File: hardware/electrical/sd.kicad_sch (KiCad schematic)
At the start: 9 parts, among them J3 Micro_SD_Card_Det2

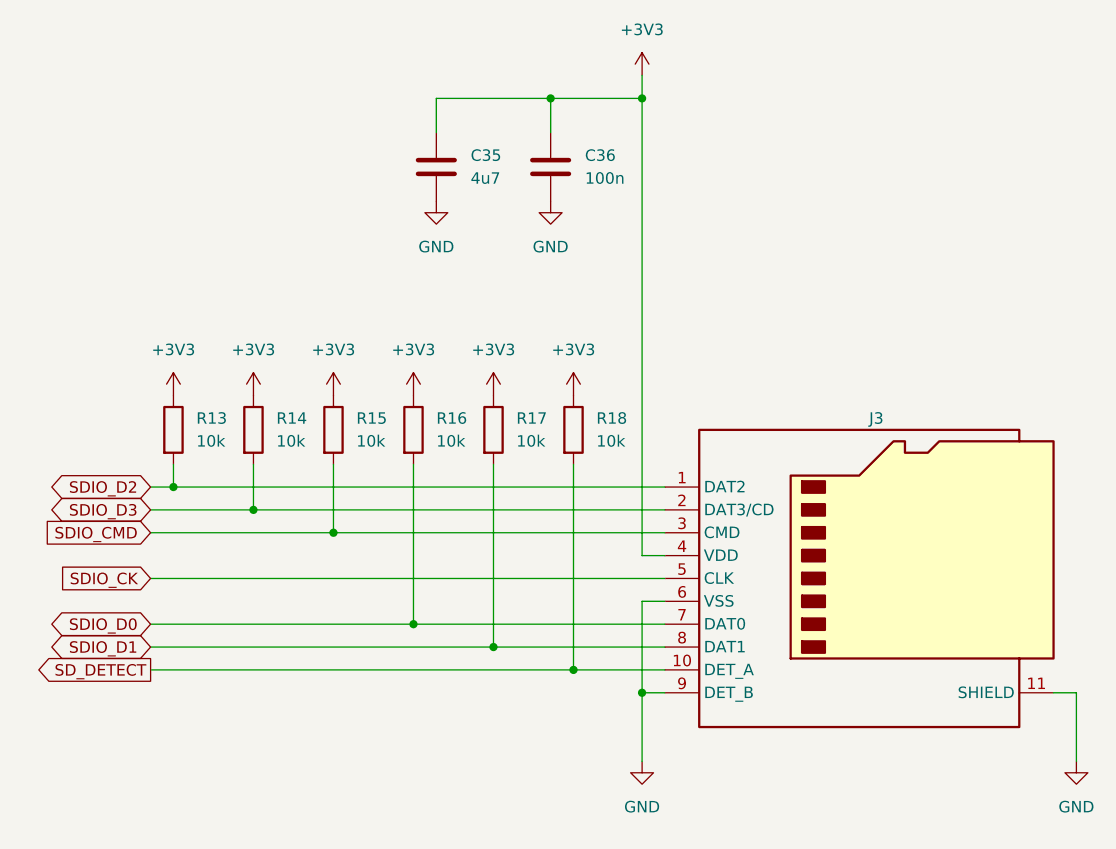
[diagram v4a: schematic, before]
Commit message: Use VDD in place of +3.3V more extensively
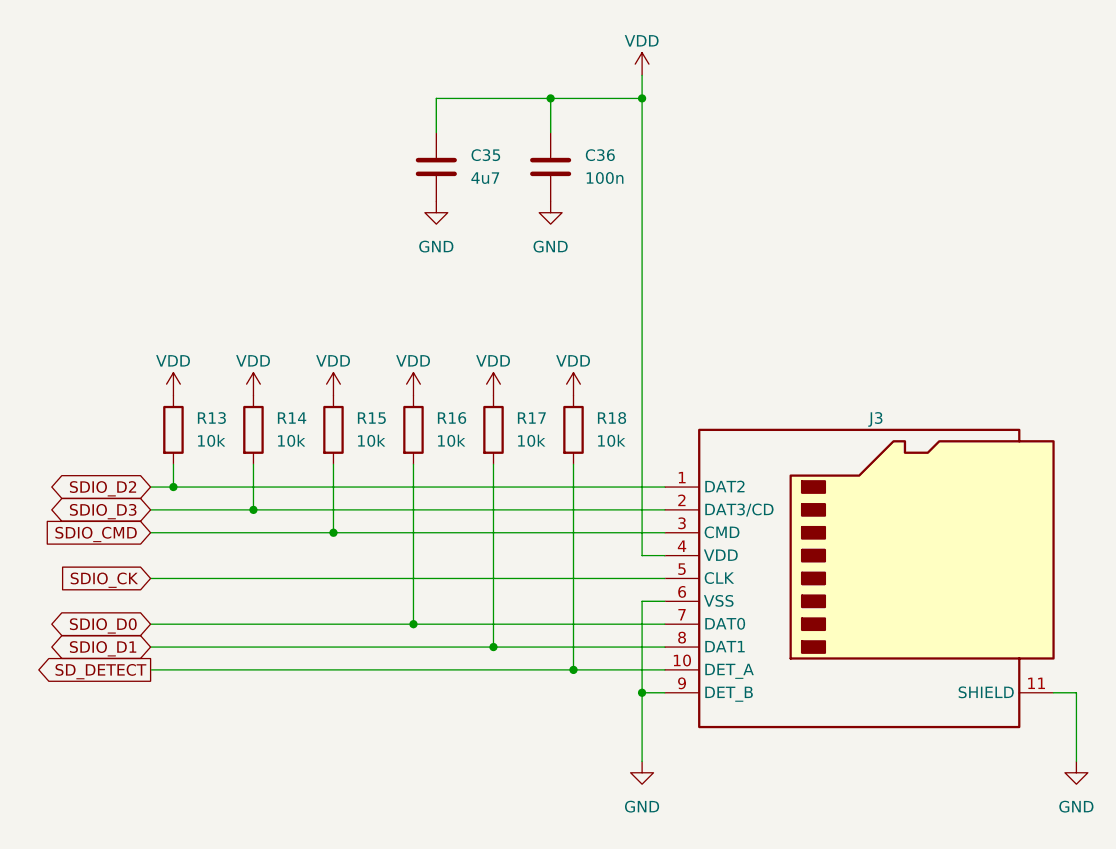
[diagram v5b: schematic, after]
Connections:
- net +3V3 renamed VDD
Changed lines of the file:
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@@
     )
   )
-  (symbol (lib_id "power:+3V3") (at 140.97 88.9 0) (unit 1)
-    (in_bom yes) (on_board yes) (dnp no)
-    (property "Reference" "#PWR060" (at 140.97 92.71 0)
-      (effects (font (size 1.27 1.27)) hide)
-    )
-    (property "Value" "+3V3" (at 140.97 83.82 0)
-      (effects (font (size 1.27 1.27)))
-    )
-    (property "Footprint" "" (at 140.97 88.9 0)
-      (effects (font (size 1.27 1.27)) hide)
-    )
-    (property "Datasheet" "" (at 140.97 88.9 0)
-      (effects (font (size 1.27 1.27)) hide)
-    )
-    (pin "1")
-    (instances
-      (project "3885"
-        (path "/7363a4f0-2da1-4086-abed-ea6709c3a185/6cde842e-a6be-40ad-bea6-4575bf07edd2"
-          (reference "#PWR060") (unit 1)
+  (symbol (lib_id "power:VDD") (at 114.3 88.9 0) (unit 1)
+    (in_bom yes) (on_board yes) (dnp no) (fields_autoplaced)
+    (property "Reference" "#PWR056" (at 114.3 92.71 0)
+      (effects (font (size 1.27 1.27)) hide)
+    )
+    (property "Value" "VDD" (at 114.3 85.09 0)
+      (effects (font (size 1.27 1.27)))
+    )
+    (property "Footprint" "" (at 114.3 88.9 0)
+      (effects (font (size 1.27 1.27)) hide)
+    )
+    (property "Datasheet" "" (at 114.3 88.9 0)
+      (effects (font (size 1.27 1.27)) hide)
+    )
+    (pin "1")
+    (instances
+      (project "3885"
+        (path "/7363a4f0-2da1-4086-abed-ea6709c3a185/6cde842e-a6be-40ad-bea6-4575bf07edd2"
+          (reference "#PWR056") (unit 1)
         )
       )
@@
     )
   )
+  (symbol (lib_id "power:VDD") (at 149.86 88.9 0) (unit 1)
+    (in_bom yes) (on_board yes) (dnp no) (fields_autoplaced)
+    (property "Reference" "#PWR062" (at 149.86 92.71 0)
+      (effects (font (size 1.27 1.27)) hide)
+    )
+    (property "Value" "VDD" (at 149.86 85.09 0)
+      (effects (font (size 1.27 1.27)))
+    )
+    (property "Footprint" "" (at 149.86 88.9 0)
+      (effects (font (size 1.27 1.27)) hide)
+    )
+    (property "Datasheet" "" (at 149.86 88.9 0)
+      (effects (font (size 1.27 1.27)) hide)
+    )
+    (pin "1")
+    (instances
+      (project "3885"
+        (path "/7363a4f0-2da1-4086-abed-ea6709c3a185/6cde842e-a6be-40ad-bea6-4575bf07edd2"
+          (reference "#PWR062") (unit 1)
+        )
+      )
+    )
+  )
   (symbol (lib_id "Device:R") (at 105.41 92.71 0) (unit 1)
     (in_bom yes) (on_board yes) (dnp no) (fields_autoplaced)
@@
     )
   )
+  (symbol (lib_id "power:VDD") (at 105.41 88.9 0) (unit 1)
+    (in_bom yes) (on_board yes) (dnp no) (fields_autoplaced)
+    (property "Reference" "#PWR055" (at 105.41 92.71 0)
+      (effects (font (size 1.27 1.27)) hide)
+    )
+    (property "Value" "VDD" (at 105.41 85.09 0)
+      (effects (font (size 1.27 1.27)))
+    )
+    (property "Footprint" "" (at 105.41 88.9 0)
+      (effects (font (size 1.27 1.27)) hide)
+    )
+    (property "Datasheet" "" (at 105.41 88.9 0)
+      (effects (font (size 1.27 1.27)) hide)
+    )
+    (pin "1")
+    (instances
+      (project "3885"
+        (path "/7363a4f0-2da1-4086-abed-ea6709c3a185/6cde842e-a6be-40ad-bea6-4575bf07edd2"
+          (reference "#PWR055") (unit 1)
+        )
+      )
+    )
+  )
   (symbol (lib_id "Device:R") (at 123.19 92.71 0) (unit 1)
     (in_bom yes) (on_board yes) (dnp no) (fields_autoplaced)
@@
     )
   )
+  (symbol (lib_id "power:VDD") (at 157.48 53.34 0) (unit 1)
+    (in_bom yes) (on_board yes) (dnp no) (fields_autoplaced)
+    (property "Reference" "#PWR063" (at 157.48 57.15 0)
+      (effects (font (size 1.27 1.27)) hide)
+    )
+    (property "Value" "VDD" (at 157.48 49.53 0)
+      (effects (font (size 1.27 1.27)))
+    )
+    (property "Footprint" "" (at 157.48 53.34 0)
+      (effects (font (size 1.27 1.27)) hide)
+    )
+    (property "Datasheet" "" (at 157.48 53.34 0)
+      (effects (font (size 1.27 1.27)) hide)
+    )
+    (pin "1")
+    (instances
+      (project "3885"
+        (path "/7363a4f0-2da1-4086-abed-ea6709c3a185/6cde842e-a6be-40ad-bea6-4575bf07edd2"
+          (reference "#PWR063") (unit 1)
+        )
+      )
+    )
+  )
   (symbol (lib_id "Device:R") (at 132.08 92.71 0) (unit 1)
     (in_bom yes) (on_board yes) (dnp no) (fields_autoplaced)
@@
     )
   )
-  (symbol (lib_id "power:+3V3") (at 132.08 88.9 0) (unit 1)
-    (in_bom yes) (on_board yes) (dnp no)
+  (symbol (lib_id "power:VDD") (at 132.08 88.9 0) (unit 1)
+    (in_bom yes) (on_board yes) (dnp no) (fields_autoplaced)
     (property "Reference" "#PWR058" (at 132.08 92.71 0)
       (effects (font (size 1.27 1.27)) hide)
     )
-    (property "Value" "+3V3" (at 132.08 83.82 0)
+    (property "Value" "VDD" (at 132.08 85.09 0)
       (effects (font (size 1.27 1.27)))
     )
@@
     )
   )
-  (symbol (lib_id "power:+3V3") (at 157.48 53.34 0) (unit 1)
-    (in_bom yes) (on_board yes) (dnp no) (fields_autoplaced)
-    (property "Reference" "#PWR063" (at 157.48 57.15 0)
-      (effects (font (size 1.27 1.27)) hide)
-    )
-    (property "Value" "+3V3" (at 157.48 48.26 0)
-      (effects (font (size 1.27 1.27)))
-    )
-    (property "Footprint" "" (at 157.48 53.34 0)
-      (effects (font (size 1.27 1.27)) hide)
-    )
-    (property "Datasheet" "" (at 157.48 53.34 0)
-      (effects (font (size 1.27 1.27)) hide)
-    )
-    (pin "1")
-    (instances
-      (project "3885"
-        (path "/7363a4f0-2da1-4086-abed-ea6709c3a185/6cde842e-a6be-40ad-bea6-4575bf07edd2"
-          (reference "#PWR063") (unit 1)
-        )
-      )
-    )
-  )
   (symbol (lib_id "Device:C") (at 134.62 63.5 0) (unit 1)
     (in_bom yes) (on_board yes) (dnp no) (fields_autoplaced)
@@
     )
   )
-  (symbol (lib_id "power:+3V3") (at 105.41 88.9 0) (unit 1)
-    (in_bom yes) (on_board yes) (dnp no) (fields_autoplaced)
-    (property "Reference" "#PWR055" (at 105.41 92.71 0)
-      (effects (font (size 1.27 1.27)) hide)
-    )
-    (property "Value" "+3V3" (at 105.41 83.82 0)
-      (effects (font (size 1.27 1.27)))
-    )
-    (property "Footprint" "" (at 105.41 88.9 0)
-      (effects (font (size 1.27 1.27)) hide)
-    )
-    (property "Datasheet" "" (at 105.41 88.9 0)
-      (effects (font (size 1.27 1.27)) hide)
-    )
-    (pin "1")
-    (instances
-      (project "3885"
-        (path "/7363a4f0-2da1-4086-abed-ea6709c3a185/6cde842e-a6be-40ad-bea6-4575bf07edd2"
-          (reference "#PWR055") (unit 1)
+  (symbol (lib_id "power:VDD") (at 140.97 88.9 0) (unit 1)
+    (in_bom yes) (on_board yes) (dnp no) (fields_autoplaced)
+    (property "Reference" "#PWR060" (at 140.97 92.71 0)
+      (effects (font (size 1.27 1.27)) hide)
+    )
+    (property "Value" "VDD" (at 140.97 85.09 0)
+      (effects (font (size 1.27 1.27)))
+    )
+    (property "Footprint" "" (at 140.97 88.9 0)
+      (effects (font (size 1.27 1.27)) hide)
+    )
+    (property "Datasheet" "" (at 140.97 88.9 0)
+      (effects (font (size 1.27 1.27)) hide)
+    )
+    (pin "1")
+    (instances
+      (project "3885"
+        (path "/7363a4f0-2da1-4086-abed-ea6709c3a185/6cde842e-a6be-40ad-bea6-4575bf07edd2"
+          (reference "#PWR060") (unit 1)
         )
       )
@@
     )
   )
-  (symbol (lib_id "power:+3V3") (at 114.3 88.9 0) (unit 1)
-    (in_bom yes) (on_board yes) (dnp no) (fields_autoplaced)
-    (property "Reference" "#PWR056" (at 114.3 92.71 0)
-      (effects (font (size 1.27 1.27)) hide)
-    )
-    (property "Value" "+3V3" (at 114.3 83.82 0)
-      (effects (font (size 1.27 1.27)))
-    )
-    (property "Footprint" "" (at 114.3 88.9 0)
-      (effects (font (size 1.27 1.27)) hide)
-    )
-    (property "Datasheet" "" (at 114.3 88.9 0)
-      (effects (font (size 1.27 1.27)) hide)
-    )
-    (pin "1")
-    (instances
-      (project "3885"
-        (path "/7363a4f0-2da1-4086-abed-ea6709c3a185/6cde842e-a6be-40ad-bea6-4575bf07edd2"
-          (reference "#PWR056") (unit 1)
+  (symbol (lib_id "power:VDD") (at 123.19 88.9 0) (unit 1)
+    (in_bom yes) (on_board yes) (dnp no) (fields_autoplaced)
+    (property "Reference" "#PWR057" (at 123.19 92.71 0)
+      (effects (font (size 1.27 1.27)) hide)
+    )
+    (property "Value" "VDD" (at 123.19 85.09 0)
+      (effects (font (size 1.27 1.27)))
+    )
+    (property "Footprint" "" (at 123.19 88.9 0)
+      (effects (font (size 1.27 1.27)) hide)
+    )
+    (property "Datasheet" "" (at 123.19 88.9 0)
+      (effects (font (size 1.27 1.27)) hide)
+    )
+    (pin "1")
+    (instances
+      (project "3885"
+        (path "/7363a4f0-2da1-4086-abed-ea6709c3a185/6cde842e-a6be-40ad-bea6-4575bf07edd2"
+          (reference "#PWR057") (unit 1)
         )
       )
@@
         )
       )
-    )
-  )
-  (symbol (lib_id "power:+3V3") (at 149.86 88.9 0) (unit 1)
-    (in_bom yes) (on_board yes) (dnp no)
-    (property "Reference" "#PWR062" (at 149.86 92.71 0)
-      (effects (font (size 1.27 1.27)) hide)
-    )
-    (property "Value" "+3V3" (at 149.86 83.82 0)
-      (effects (font (size 1.27 1.27)))
-    )
-    (property "Footprint" "" (at 149.86 88.9 0)
-      (effects (font (size 1.27 1.27)) hide)
-    )
-    (property "Datasheet" "" (at 149.86 88.9 0)
-      (effects (font (size 1.27 1.27)) hide)
-    )
-    (pin "1")
-    (instances
-      (project "3885"
-        (path "/7363a4f0-2da1-4086-abed-ea6709c3a185/6cde842e-a6be-40ad-bea6-4575bf07edd2"
-          (reference "#PWR062") (unit 1)
-        )
-      )
-    )
-  )
-  (symbol (lib_id "power:+3V3") (at 123.19 88.9 0) (unit 1)
-    (in_bom yes) (on_board yes) (dnp no) (fields_autoplaced)
-    (property "Reference" "#PWR057" (at 123.19 92.71 0)
-      (effects (font (size 1.27 1.27)) hide)
-    )
-    (property "Value" "+3V3" (at 123.19 83.82 0)
-      (effects (font (size 1.27 1.27)))
-    )
-    (property "Footprint" "" (at 123.19 88.9 0)
-      (effects (font (size 1.27 1.27)) hide)
-    )
-    (property "Datasheet" "" (at 123.19 88.9 0)
-      (effects (font (size 1.27 1.27)) hide)
-    )
-    (pin "1")
-    (instances
-      (project "3885"
-        (path "/7363a4f0-2da1-4086-abed-ea6709c3a185/6cde842e-a6be-40ad-bea6-4575bf07edd2"
-          (reference "#PWR057") (unit 1)
-        )
-      )

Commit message: Component selection
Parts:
- C35: footprint (none) -> Capacitor_SMD:C_0402_1005Metric; LCSC Part # (none) -> C23733; Mfr (none) -> Samsung Electro-Mechanics; Mfr. Part # (none) -> CL05A475MP5NRNC
- C36: footprint (none) -> Capacitor_SMD:C_0402_1005Metric; LCSC Part # (none) -> C1525; Mfr (none) -> Samsung Electro-Mechanics; Mfr. Part # (none) -> CL05B104KO5NNNC
- J3: LCSC Part # (none) -> C381084; Mfr (none) -> XKB Connectivity; Mfr. Part # (none) -> XKTF-N02-N
- R13, R14, R15, R16, R17, R18: footprint (none) -> Resistor_SMD:R_0402_1005Metric; LCSC Part # (none) -> C25744; Mfr (none) -> UNI-ROYAL(Uniroyal Elec); Mfr. Part # (none) -> 0402WGF1002TCE
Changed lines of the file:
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@@
       (effects (font (size 1.27 1.27)) (justify left))
     )
-    (property "Footprint" "" (at 103.632 92.71 90)
-      (effects (font (size 1.27 1.27)) hide)
-    )
-    (property "Datasheet" "~" (at 105.41 92.71 0)
+    (property "Footprint" "Resistor_SMD:R_0402_1005Metric" (at 103.632 92.71 90)
+      (effects (font (size 1.27 1.27)) hide)
+    )
+    (property "Datasheet" "https://datasheet.lcsc.com/lcsc/2206010100_UNI-ROYAL-Uniroyal-Elec-0402WGF1002TCE_C25744.pdf" (at 105.41 92.71 0)
+      (effects (font (size 1.27 1.27)) hide)
+    )
+    (property "LCSC Part #" "C25744" (at 105.41 92.71 0)
+      (effects (font (size 1.27 1.27)) hide)
+    )
+    (property "Mfr" "UNI-ROYAL(Uniroyal Elec)" (at 105.41 92.71 0)
+      (effects (font (size 1.27 1.27)) hide)
+    )
+    (property "Mfr. Part #" "0402WGF1002TCE" (at 105.41 92.71 0)
       (effects (font (size 1.27 1.27)) hide)
     )
@@
       (effects (font (size 1.27 1.27)) (justify left))
     )
-    (property "Footprint" "" (at 121.412 92.71 90)
-      (effects (font (size 1.27 1.27)) hide)
-    )
-    (property "Datasheet" "~" (at 123.19 92.71 0)
+    (property "Footprint" "Resistor_SMD:R_0402_1005Metric" (at 121.412 92.71 90)
+      (effects (font (size 1.27 1.27)) hide)
+    )
+    (property "Datasheet" "https://datasheet.lcsc.com/lcsc/2206010100_UNI-ROYAL-Uniroyal-Elec-0402WGF1002TCE_C25744.pdf" (at 123.19 92.71 0)
+      (effects (font (size 1.27 1.27)) hide)
+    )
+    (property "LCSC Part #" "C25744" (at 123.19 92.71 0)
+      (effects (font (size 1.27 1.27)) hide)
+    )
+    (property "Mfr" "UNI-ROYAL(Uniroyal Elec)" (at 123.19 92.71 0)
+      (effects (font (size 1.27 1.27)) hide)
+    )
+    (property "Mfr. Part #" "0402WGF1002TCE" (at 123.19 92.71 0)
       (effects (font (size 1.27 1.27)) hide)
     )
@@
       (effects (font (size 1.27 1.27)) (justify left))
     )
-    (property "Footprint" "" (at 130.302 92.71 90)
-      (effects (font (size 1.27 1.27)) hide)
-    )
-    (property "Datasheet" "~" (at 132.08 92.71 0)
+    (property "Footprint" "Resistor_SMD:R_0402_1005Metric" (at 130.302 92.71 90)
+      (effects (font (size 1.27 1.27)) hide)
+    )
+    (property "Datasheet" "https://datasheet.lcsc.com/lcsc/2206010100_UNI-ROYAL-Uniroyal-Elec-0402WGF1002TCE_C25744.pdf" (at 132.08 92.71 0)
+      (effects (font (size 1.27 1.27)) hide)
+    )
+    (property "LCSC Part #" "C25744" (at 132.08 92.71 0)
+      (effects (font (size 1.27 1.27)) hide)
+    )
+    (property "Mfr" "UNI-ROYAL(Uniroyal Elec)" (at 132.08 92.71 0)
+      (effects (font (size 1.27 1.27)) hide)
+    )
+    (property "Mfr. Part #" "0402WGF1002TCE" (at 132.08 92.71 0)
       (effects (font (size 1.27 1.27)) hide)
     )
@@
       (effects (font (size 1.27 1.27)) hide)
     )
-    (property "Datasheet" "https://www.hirose.com/en/product/document?clcode=&productname=&series=DM3&documenttype=Catalog&lang=en&documentid=D49662_en" (at 185.42 106.68 0)
+    (property "Datasheet" "https://datasheet.lcsc.com/lcsc/2110151630_XKB-Connectivity-XKTF-N02-N_C381084.pdf" (at 185.42 106.68 0)
+      (effects (font (size 1.27 1.27)) hide)
+    )
+    (property "LCSC Part #" "C381084" (at 182.88 109.22 0)
+      (effects (font (size 1.27 1.27)) hide)
+    )
+    (property "Mfr" "XKB Connectivity" (at 182.88 109.22 0)
+      (effects (font (size 1.27 1.27)) hide)
+    )
+    (property "Mfr. Part #" "XKTF-N02-N" (at 182.88 109.22 0)
       (effects (font (size 1.27 1.27)) hide)
     )
@@
       (effects (font (size 1.27 1.27)) (justify left))
     )
-    (property "Footprint" "" (at 135.5852 67.31 0)
-      (effects (font (size 1.27 1.27)) hide)
-    )
-    (property "Datasheet" "~" (at 134.62 63.5 0)
+    (property "Footprint" "Capacitor_SMD:C_0402_1005Metric" (at 135.5852 67.31 0)
+      (effects (font (size 1.27 1.27)) hide)
+    )
+    (property "Datasheet" "https://datasheet.lcsc.com/lcsc/1810191211_Samsung-Electro-Mechanics-CL05A475MP5NRNC_C23733.pdf" (at 134.62 63.5 0)
+      (effects (font (size 1.27 1.27)) hide)
+    )
+    (property "LCSC Part #" "C23733" (at 134.62 63.5 0)
+      (effects (font (size 1.27 1.27)) hide)
+    )
+    (property "Mfr" "Samsung Electro-Mechanics" (at 134.62 63.5 0)
+      (effects (font (size 1.27 1.27)) hide)
+    )
+    (property "Mfr. Part #" "CL05A475MP5NRNC" (at 134.62 63.5 0)
       (effects (font (size 1.27 1.27)) hide)
     )
@@
       (effects (font (size 1.27 1.27)) (justify left))
     )
-    (property "Footprint" "" (at 148.2852 67.31 0)
-      (effects (font (size 1.27 1.27)) hide)
-    )
-    (property "Datasheet" "~" (at 147.32 63.5 0)
+    (property "Footprint" "Capacitor_SMD:C_0402_1005Metric" (at 148.2852 67.31 0)
+      (effects (font (size 1.27 1.27)) hide)
+    )
+    (property "Datasheet" "https://datasheet.lcsc.com/lcsc/1810191219_Samsung-Electro-Mechanics-CL05B104KO5NNNC_C1525.pdf" (at 147.32 63.5 0)
+      (effects (font (size 1.27 1.27)) hide)
+    )
+    (property "LCSC Part #" "C1525" (at 147.32 63.5 0)
+      (effects (font (size 1.27 1.27)) hide)
+    )
+    (property "Mfr" "Samsung Electro-Mechanics" (at 147.32 63.5 0)
+      (effects (font (size 1.27 1.27)) hide)
+    )
+    (property "Mfr. Part #" "CL05B104KO5NNNC" (at 147.32 63.5 0)
       (effects (font (size 1.27 1.27)) hide)
     )
@@
       (effects (font (size 1.27 1.27)) (justify left))
     )
-    (property "Footprint" "" (at 112.522 92.71 90)
-      (effects (font (size 1.27 1.27)) hide)
-    )
-    (property "Datasheet" "~" (at 114.3 92.71 0)
+    (property "Footprint" "Resistor_SMD:R_0402_1005Metric" (at 112.522 92.71 90)
+      (effects (font (size 1.27 1.27)) hide)
+    )
+    (property "Datasheet" "https://datasheet.lcsc.com/lcsc/2206010100_UNI-ROYAL-Uniroyal-Elec-0402WGF1002TCE_C25744.pdf" (at 114.3 92.71 0)
+      (effects (font (size 1.27 1.27)) hide)
+    )
+    (property "LCSC Part #" "C25744" (at 114.3 92.71 0)
+      (effects (font (size 1.27 1.27)) hide)
+    )
+    (property "Mfr" "UNI-ROYAL(Uniroyal Elec)" (at 114.3 92.71 0)
+      (effects (font (size 1.27 1.27)) hide)
+    )
+    (property "Mfr. Part #" "0402WGF1002TCE" (at 114.3 92.71 0)
       (effects (font (size 1.27 1.27)) hide)
     )
@@
       (effects (font (size 1.27 1.27)) (justify left))
     )
-    (property "Footprint" "" (at 148.082 92.71 90)
-      (effects (font (size 1.27 1.27)) hide)
-    )
-    (property "Datasheet" "~" (at 149.86 92.71 0)
+    (property "Footprint" "Resistor_SMD:R_0402_1005Metric" (at 148.082 92.71 90)
+      (effects (font (size 1.27 1.27)) hide)
+    )
+    (property "Datasheet" "https://datasheet.lcsc.com/lcsc/2206010100_UNI-ROYAL-Uniroyal-Elec-0402WGF1002TCE_C25744.pdf" (at 149.86 92.71 0)
+      (effects (font (size 1.27 1.27)) hide)
+    )
+    (property "LCSC Part #" "C25744" (at 149.86 92.71 0)
+      (effects (font (size 1.27 1.27)) hide)
+    )
+    (property "Mfr" "UNI-ROYAL(Uniroyal Elec)" (at 149.86 92.71 0)
+      (effects (font (size 1.27 1.27)) hide)
+    )
+    (property "Mfr. Part #" "0402WGF1002TCE" (at 149.86 92.71 0)
       (effects (font (size 1.27 1.27)) hide)
     )
@@
       (effects (font (size 1.27 1.27)) (justify left))
     )
-    (property "Footprint" "" (at 139.192 92.71 90)
-      (effects (font (size 1.27 1.27)) hide)
-    )
-    (property "Datasheet" "~" (at 140.97 92.71 0)
-      (effects (font (size 1.27 1.27)) hide)
-    )
+    (property "Footprint" "Resistor_SMD:R_0402_1005Metric" (at 139.192 92.71 90)
+      (effects (font (size 1.27 1.27)) hide)
+    )
+    (property "Datasheet" "https://datasheet.lcsc.com/lcsc/2206010100_UNI-ROYAL-Uniroyal-Elec-0402WGF1002TCE_C25744.pdf" (at 140.97 92.71 0)
+      (effects (font (size 1.27 1.27)) hide)
+    )
+    (property "LCSC Part #" "C25744" (at 140.97 92.71 0)
+      (effects (font (size 1.27 1.27)) hide)
+    )
+    (property "Mfr" "UNI-ROYAL(Uniroyal Elec)" (at 140.97 92.71 0)
+      (effects (font (size 1.27 1.27)) hide)
+    )
+    (property "Mfr. Part #" "0402WGF1002TCE" (at 140.97 92.71 0)
+      (effects (font (size 1.27 1.27)) hide)
+    )
